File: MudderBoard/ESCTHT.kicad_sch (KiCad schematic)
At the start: 82 parts, among them M3 N-MOSFET, M4 N-MOSFET, U8 LM5122QMH/NOPB, U9 LM5122QMH/NOPB

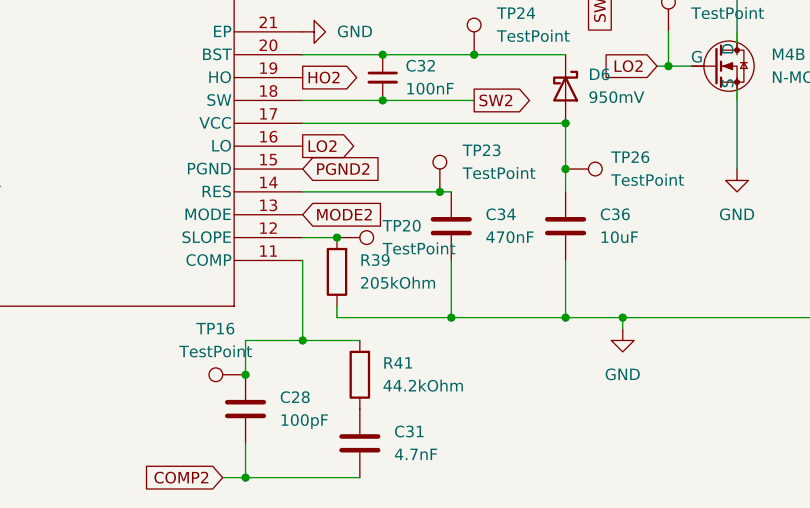
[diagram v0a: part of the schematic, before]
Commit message: Preliminary ESC Boost Layout
Arranged footprints and test points. Still need to route but waiting to see how many layers etc.
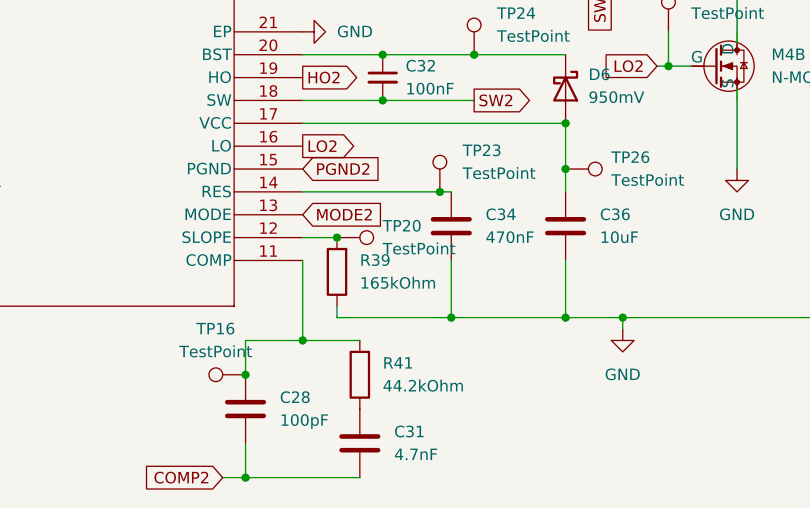
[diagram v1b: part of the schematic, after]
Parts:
- R39: value 205kOhm -> 165kOhm
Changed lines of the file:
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@@
 	)
 	(junction
-		(at 176.53 137.16)
-		(diameter 0)
-		(color 0 0 0 0)
-	)
-	(junction
 		(at 240.03 100.33)
 		(diameter 0)
@@
 	)
 	(junction
+		(at 176.53 137.16)
+		(diameter 0)
+		(color 0 0 0 0)
+	)
+	(junction
 		(at 248.92 26.67)
 		(diameter 0)
@@
 	)
 	(symbol
+		(lib_id "Device:R")
+		(at 176.53 140.97 180)
+		(unit 1)
+		(exclude_from_sim no)
+		(in_bom yes)
+		(on_board yes)
+		(dnp no)
+		(fields_autoplaced yes)
+		(property "Reference" "R39"
+			(at 179.07 139.6999 0)
+			(effects
+				(font
+					(size 1.27 1.27)
+				)
+				(justify right)
+			)
+		)
+		(property "Value" "165kOhm"
+			(at 179.07 142.2399 0)
+			(effects
+				(font
+					(size 1.27 1.27)
+				)
+				(justify right)
+			)
+		)
+		(property "Footprint" "Lidar_Foot:RESC1005X40N"
+			(at 178.308 140.97 90)
+			(effects
+				(font
+					(size 1.27 1.27)
+				)
+				(hide yes)
+			)
+		)
+		(property "Datasheet" "~"
+			(at 176.53 140.97 0)
+			(effects
+				(font
+					(size 1.27 1.27)
+				)
+				(hide yes)
+			)
+		)
+		(property "Description" "Resistor"
+			(at 176.53 140.97 0)
+			(effects
+				(font
+					(size 1.27 1.27)
+				)
+				(hide yes)
+			)
+		)
+		(pin "1"
+		)
+		(pin "2"
+		)
+		(instances
+			(project "MudderBoard"
+				(path "/cdf98bf7-80ce-4b13-b655-e6c7c589c122/156878a8-0263-42d4-a037-3f42ee3dc0ef"
+					(reference "R39")
+					(unit 1)
+				)
+			)
+		)
+	)
+	(symbol
 		(lib_id "Connector:TestPoint")
 		(at 58.42 128.27 90)
@@
 					(unit 1)
 				)
-			)
-		)
-	)
-	(symbol
-		(lib_id "Device:R")
-		(at 176.53 140.97 180)
-		(unit 1)
-		(exclude_from_sim no)
-		(in_bom yes)
-		(on_board yes)
-		(dnp no)
-		(fields_autoplaced yes)
-		(property "Reference" "R39"
-			(at 179.07 139.6999 0)
-			(effects
-				(font
-					(size 1.27 1.27)
-				)
-				(justify right)
-			)
-		)
-		(property "Value" "205kOhm"
-			(at 179.07 142.2399 0)
-			(effects
-				(font
-					(size 1.27 1.27)
-				)
-				(justify right)
-			)
-		)
-		(property "Footprint" "Lidar_Foot:RESC1005X40N"
-			(at 178.308 140.97 90)
-			(effects
-				(font
-					(size 1.27 1.27)
-				)
-				(hide yes)
-			)
-		)
-		(property "Datasheet" "~"
-			(at 176.53 140.97 0)
-			(effects
-				(font
-					(size 1.27 1.27)
-				)
-				(hide yes)
-			)
-		)
-		(property "Description" "Resistor"
-			(at 176.53 140.97 0)
-			(effects
-				(font
-					(size 1.27 1.27)
-				)
-				(hide yes)
-			)
-		)
-		(pin "1"
-		)
-		(pin "2"
-		)
-		(instances
-			(project "MudderBoard"
-				(path "/cdf98bf7-80ce-4b13-b655-e6c7c589c122/156878a8-0263-42d4-a037-3f42ee3dc0ef"
-					(reference "R39")
-					(unit 1)
-				)

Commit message: revert to colin changes
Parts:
- R39: value 165kOhm -> 205kOhm
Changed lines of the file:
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@@
 	)
 	(junction
+		(at 176.53 137.16)
+		(diameter 0)
+		(color 0 0 0 0)
+	)
+	(junction
 		(at 240.03 100.33)
 		(diameter 0)
@@
 	)
 	(junction
-		(at 176.53 137.16)
-		(diameter 0)
-		(color 0 0 0 0)
-	)
-	(junction
 		(at 248.92 26.67)
 		(diameter 0)
@@
 	)
 	(symbol
-		(lib_id "Device:R")
-		(at 176.53 140.97 180)
-		(unit 1)
-		(exclude_from_sim no)
-		(in_bom yes)
-		(on_board yes)
-		(dnp no)
-		(fields_autoplaced yes)
-		(property "Reference" "R39"
-			(at 179.07 139.6999 0)
-			(effects
-				(font
-					(size 1.27 1.27)
-				)
-				(justify right)
-			)
-		)
-		(property "Value" "165kOhm"
-			(at 179.07 142.2399 0)
-			(effects
-				(font
-					(size 1.27 1.27)
-				)
-				(justify right)
-			)
-		)
-		(property "Footprint" "Lidar_Foot:RESC1005X40N"
-			(at 178.308 140.97 90)
-			(effects
-				(font
-					(size 1.27 1.27)
-				)
-				(hide yes)
-			)
-		)
-		(property "Datasheet" "~"
-			(at 176.53 140.97 0)
-			(effects
-				(font
-					(size 1.27 1.27)
-				)
-				(hide yes)
-			)
-		)
-		(property "Description" "Resistor"
-			(at 176.53 140.97 0)
-			(effects
-				(font
-					(size 1.27 1.27)
-				)
-				(hide yes)
-			)
-		)
-		(pin "1"
-		)
-		(pin "2"
-		)
-		(instances
-			(project "MudderBoard"
-				(path "/cdf98bf7-80ce-4b13-b655-e6c7c589c122/156878a8-0263-42d4-a037-3f42ee3dc0ef"
-					(reference "R39")
-					(unit 1)
-				)
-			)
-		)
-	)
-	(symbol
 		(lib_id "Connector:TestPoint")
 		(at 58.42 128.27 90)
@@
 					(unit 1)
 				)
+			)
+		)
+	)
+	(symbol
+		(lib_id "Device:R")
+		(at 176.53 140.97 180)
+		(unit 1)
+		(exclude_from_sim no)
+		(in_bom yes)
+		(on_board yes)
+		(dnp no)
+		(fields_autoplaced yes)
+		(property "Reference" "R39"
+			(at 179.07 139.6999 0)
+			(effects
+				(font
+					(size 1.27 1.27)
+				)
+				(justify right)
+			)
+		)
+		(property "Value" "205kOhm"
+			(at 179.07 142.2399 0)
+			(effects
+				(font
+					(size 1.27 1.27)
+				)
+				(justify right)
+			)
+		)
+		(property "Footprint" "Lidar_Foot:RESC1005X40N"
+			(at 178.308 140.97 90)
+			(effects
+				(font
+					(size 1.27 1.27)
+				)
+				(hide yes)
+			)
+		)
+		(property "Datasheet" "~"
+			(at 176.53 140.97 0)
+			(effects
+				(font
+					(size 1.27 1.27)
+				)
+				(hide yes)
+			)
+		)
+		(property "Description" "Resistor"
+			(at 176.53 140.97 0)
+			(effects
+				(font
+					(size 1.27 1.27)
+				)
+				(hide yes)
+			)
+		)
+		(pin "1"
+		)
+		(pin "2"
+		)
+		(instances
+			(project "MudderBoard"
+				(path "/cdf98bf7-80ce-4b13-b655-e6c7c589c122/156878a8-0263-42d4-a037-3f42ee3dc0ef"
+					(reference "R39")
+					(unit 1)
+				)

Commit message: Layout
ESC
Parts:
- removed M3, M4: N-MOSFET, Lidar_Foot:TRANS_CSD17308Q3, symbol DI110N04PQ-AQ:nMOS
- added Q3, Q4, Q5, Q7: CSD16340Q3, ColinFET1:TRANS_CSD16340Q3, symbol ColinFET1:CSD16340Q3
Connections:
- net ESC1: now also Q3.5-8
- net ESC2: now also Q4.5-8
- net GND: now also Q5.1, Q7.1
- net HO: now also TP29.1, Q3.4
- net HO2: now also Q4.4
- net LO: now also Q7.4
- net LO2: now also Q5.4
- net SW: now also Q3.1, Q7.5-8
- net SW2: now also Q4.1, Q5.5-8
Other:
- moved on the sheet: TP27, TP29, TP30
